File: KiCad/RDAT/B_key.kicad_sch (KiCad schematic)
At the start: 29 parts

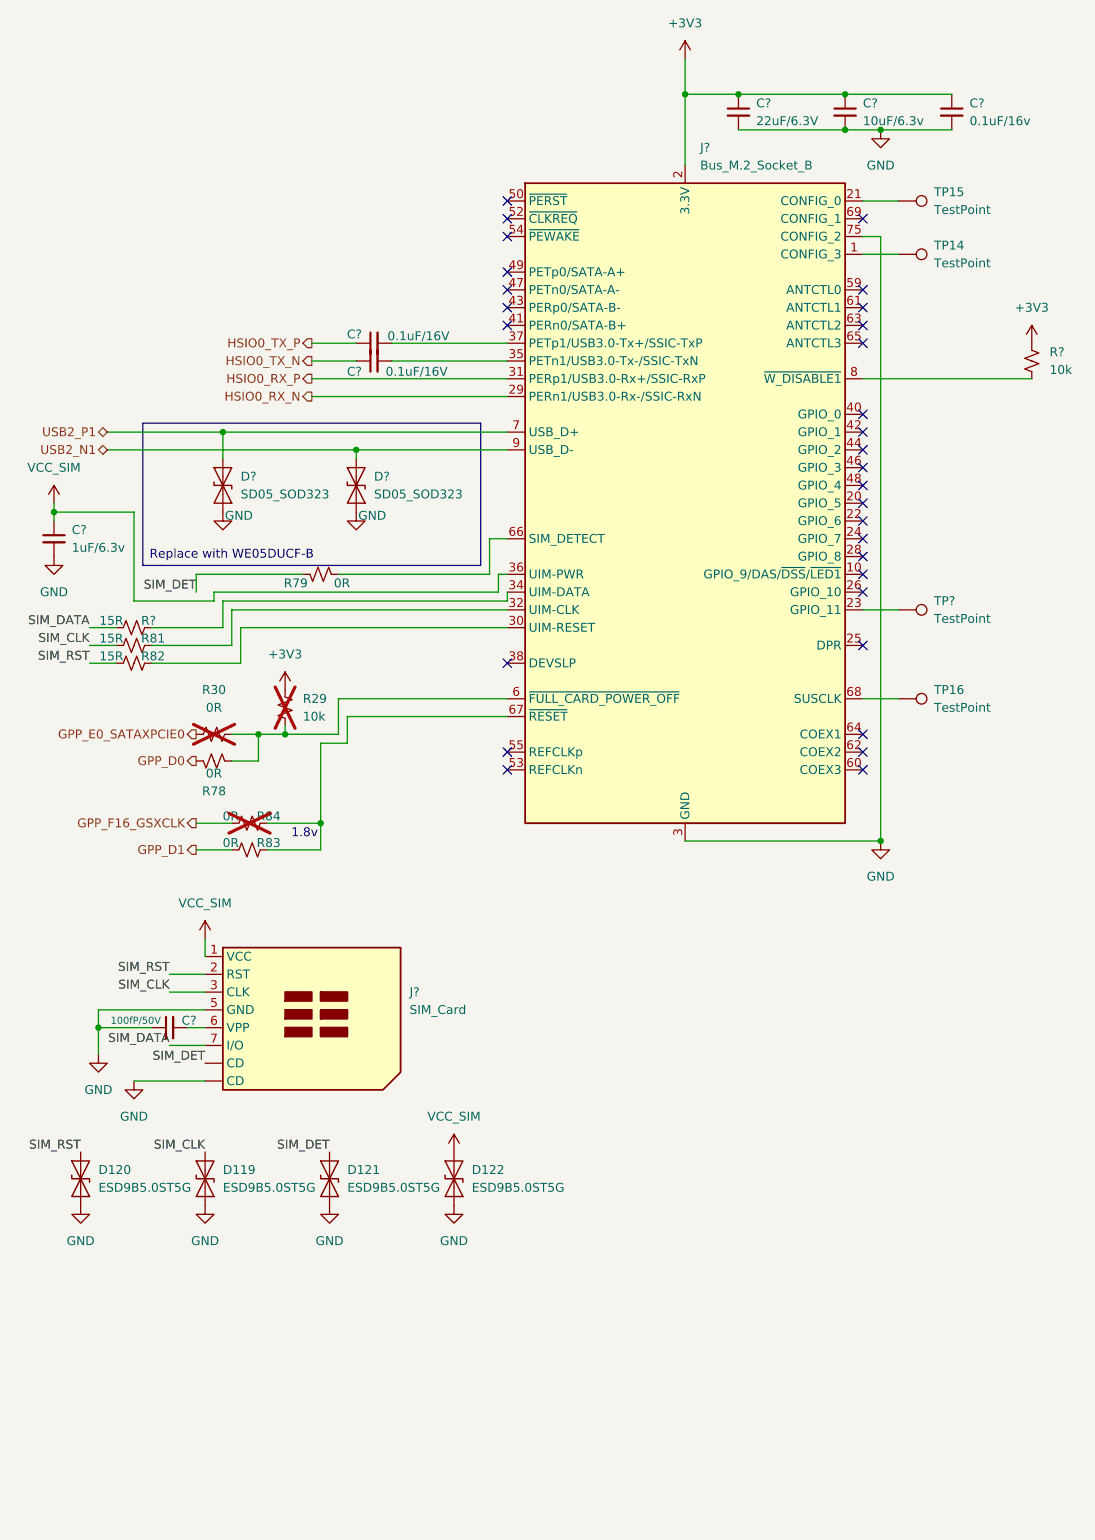
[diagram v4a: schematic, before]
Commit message: Added Libs and DOCS
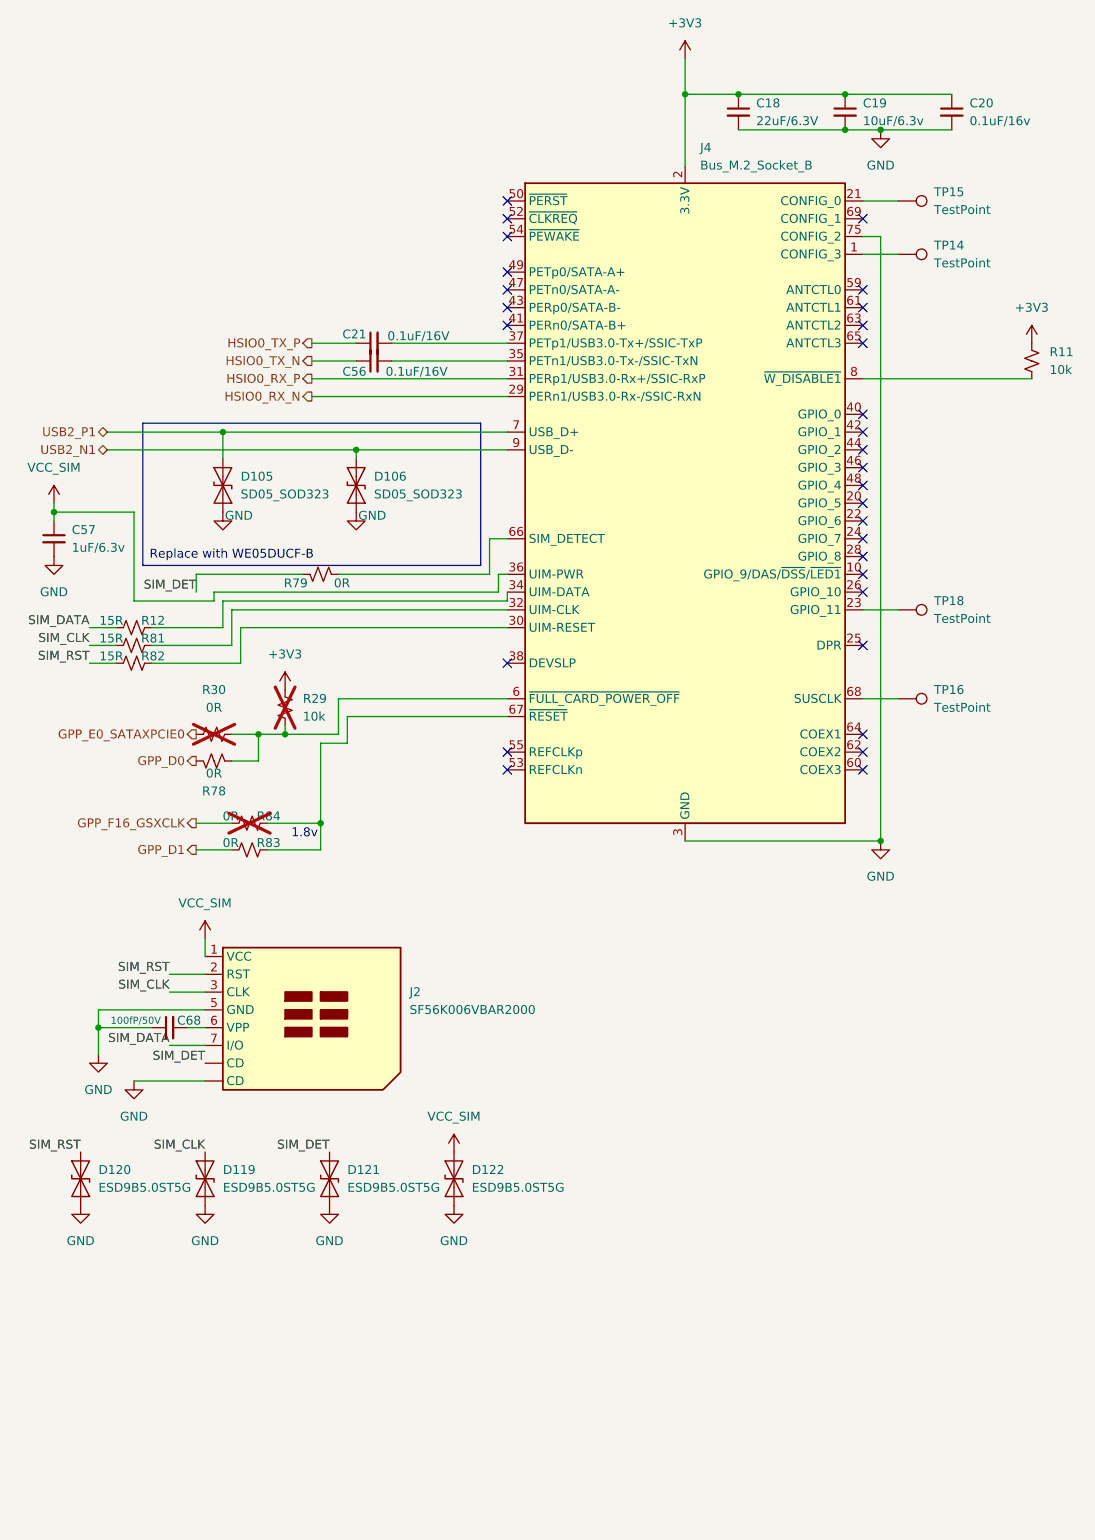
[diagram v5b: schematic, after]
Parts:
- J2: renamed from J?; value SIM_Card -> SF56K006VBAR2000; footprint (none) -> footprints:SF72S006VBDR2500_JAE; JLCPCB_LINK (none) -> https://jlcpcb.com/partdetail/JAEElectronics-SF56K006VBAR20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
- J4: renamed from J?; footprint (none) -> footprints:AMPHENOL_MDT420B03001; JLCPCB_LINK (none) -> https://jlcpcb.com/partdetail/AmphenolICC-MDT420B03001/C488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
- gave numbers to parts that had none: 12
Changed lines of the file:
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@@
 		(dnp no)
 		(fields_autoplaced yes)
-		(property "Reference" "#PWR?"
+		(property "Reference" "#PWR022"
 			(at 135.89 66.04 0)
 			(effects
@@
 			(project "RDAT"
 				(path "/0db9370a-8a21-4fd2-83a9-f207c3725dc9/55ec8a2f-3960-4a3a-93a6-0eefb6fdb74b"
-					(reference "#PWR?")
+					(reference "#PWR022")
 					(unit 1)
 				)
@@
 		(on_board yes)
 		(dnp no)
-		(property "Reference" "R?"
+		(property "Reference" "R12"
 			(at 30.226 130.556 90)
 			(effects
@@
 			(project "RDAT"
 				(path "/0db9370a-8a21-4fd2-83a9-f207c3725dc9/55ec8a2f-3960-4a3a-93a6-0eefb6fdb74b"
-					(reference "R?")
+					(reference "R12")
 					(unit 1)
 				)
@@
 		(dnp no)
 		(fields_autoplaced yes)
-		(property "Reference" "#PWR?"
+		(property "Reference" "#PWR023"
 			(at 157.48 93.98 0)
 			(effects
@@
 			(project "RDAT"
 				(path "/0db9370a-8a21-4fd2-83a9-f207c3725dc9/55ec8a2f-3960-4a3a-93a6-0eefb6fdb74b"
-					(reference "#PWR?")
+					(reference "#PWR023")
 					(unit 1)
 				)
@@
 		(dnp no)
 		(fields_autoplaced yes)
-		(property "Reference" "J?"
+		(property "Reference" "J4"
 			(at 110.0933 62.23 0)
 			(effects
@@
 			)
 		)
-		(property "Footprint" ""
+		(property "Footprint" "footprints:AMPHENOL_MDT420B03001"
 			(at 107.95 86.36 0)
 			(effects
@@
 			)
 		)
-		(property "JLCPCB_LINK" ""
+		(property "JLCPCB_LINK" "https://jlcpcb.com/partdetail/AmphenolICC-MDT420B03001/C4885179"
 			(at 107.95 113.03 0)
 			(effects
@@
 					(size 1.27 1.27)
 				)
+				(hide yes)
 			)
 		)
@@
 			(project "RDAT"
 				(path "/0db9370a-8a21-4fd2-83a9-f207c3725dc9/55ec8a2f-3960-4a3a-93a6-0eefb6fdb74b"
-					(reference "J?")
+					(reference "J4")
 					(unit 1)
 				)
@@
 		(dnp no)
 		(fields_autoplaced yes)
-		(property "Reference" "D?"
+		(property "Reference" "D106"
 			(at 63.5 109.2199 90)
 			(effects
@@
 			(project "RDAT"
 				(path "/0db9370a-8a21-4fd2-83a9-f207c3725dc9/55ec8a2f-3960-4a3a-93a6-0eefb6fdb74b"
-					(reference "D?")
+					(reference "D106")
 					(unit 1)
 				)
@@
 		(dnp no)
 		(fields_autoplaced yes)
-		(property "Reference" "J?"
+		(property "Reference" "J2"
 			(at 68.58 182.8799 0)
 			(effects
@@
 			)
 		)
-		(property "Value" "SIM_Card"
+		(property "Value" "SF56K006VBAR2000"
 			(at 68.58 185.4199 0)
 			(effects
@@
 			)
 		)
-		(property "Footprint" ""
+		(property "Footprint" "footprints:SF72S006VBDR2500_JAE"
 			(at 52.07 176.53 0)
 			(effects
@@
 			)
 		)
-		(property "Datasheet" "~"
+		(property "Datasheet" "https://wmsc.lcsc.com/wmsc/upload/file/pdf/v2/lcsc/2302091809_JAE-Electronics-SF56K006VBAR2000_C5357112.pdf"
 			(at 50.8 185.42 0)
 			(effects
@@
 			)
 		)
-		(property "JLCPCB_LINK" ""
+		(property "JLCPCB_LINK" "https://jlcpcb.com/partdetail/JAEElectronics-SF56K006VBAR2000/C5357112"
 			(at 52.07 185.42 0)
 			(effects
@@
 					(size 1.27 1.27)
 				)
+				(hide yes)
 			)
 		)
@@
 			(project "RDAT"
 				(path "/0db9370a-8a21-4fd2-83a9-f207c3725dc9/55ec8a2f-3960-4a3a-93a6-0eefb6fdb74b"
-					(reference "J?")
+					(reference "J2")
 					(unit 1)
 				)
@@
 		(dnp no)
 		(fields_autoplaced yes)
-		(property "Reference" "C?"
+		(property "Reference" "C18"
 			(at 118.11 55.8862 0)
 			(effects
@@
 			(project "RDAT"
 				(path "/0db9370a-8a21-4fd2-83a9-f207c3725dc9/55ec8a2f-3960-4a3a-93a6-0eefb6fdb74b"
-					(reference "C?")
+					(reference "C18")
 					(unit 1)
 				)
@@
 		(dnp no)
 		(fields_autoplaced yes)
-		(property "Reference" "C?"
+		(property "Reference" "C19"
 			(at 133.35 55.8862 0)
 			(effects
@@
 			(project "RDAT"
 				(path "/0db9370a-8a21-4fd2-83a9-f207c3725dc9/55ec8a2f-3960-4a3a-93a6-0eefb6fdb74b"
-					(reference "C?")
+					(reference "C19")
 					(unit 1)
 				)
@@
 		(dnp no)
 		(fields_autoplaced yes)
-		(property "Reference" "#PWR?"
+		(property "Reference" "#PWR028"
 			(at 135.89 167.64 0)
 			(effects
@@
 			(project "RDAT"
 				(path "/0db9370a-8a21-4fd2-83a9-f207c3725dc9/55ec8a2f-3960-4a3a-93a6-0eefb6fdb74b"
-					(reference "#PWR?")
+					(reference "#PWR028")
 					(unit 1)
 				)
@@
 		(dnp no)
 		(fields_autoplaced yes)
-		(property "Reference" "#PWR?"
+		(property "Reference" "#PWR024"
 			(at 17.78 116.84 0)
 			(effects
@@
 			(project "RDAT"
 				(path "/0db9370a-8a21-4fd2-83a9-f207c3725dc9/55ec8a2f-3960-4a3a-93a6-0eefb6fdb74b"
-					(reference "#PWR?")
+					(reference "#PWR024")
 					(unit 1)
 				)
@@
 		(dnp no)
 		(fields_autoplaced yes)
-		(property "Reference" "#PWR?"
+		(property "Reference" "#PWR027"
 			(at 17.78 127 0)
 			(effects
@@
 			(project "RDAT"
 				(path "/0db9370a-8a21-4fd2-83a9-f207c3725dc9/55ec8a2f-3960-4a3a-93a6-0eefb6fdb74b"
-					(reference "#PWR?")
+					(reference "#PWR027")
 					(unit 1)
 				)
@@
 		(dnp no)
 		(fields_autoplaced yes)
-		(property "Reference" "C?"
+		(property "Reference" "C57"
 			(at 20.32 116.8462 0)
 			(effects
@@
 			(project "RDAT"
 				(path "/0db9370a-8a21-4fd2-83a9-f207c3725dc9/55ec8a2f-3960-4a3a-93a6-0eefb6fdb74b"
-					(reference "C?")
+					(reference "C57")
 					(unit 1)
 				)
@@
 		(dnp no)
 		(fields_autoplaced yes)
-		(property "Reference" "C?"
+		(property "Reference" "C20"
 			(at 148.59 55.8862 0)
 			(effects
@@
 			(project "RDAT"
 				(path "/0db9370a-8a21-4fd2-83a9-f207c3725dc9/55ec8a2f-3960-4a3a-93a6-0eefb6fdb74b"
-					(reference "C?")
+					(reference "C20")
 					(unit 1)
 				)
@@
 		(on_board yes)
 		(dnp no)
-		(property "Reference" "C?"
+		(property "Reference" "C56"
 			(at 60.706 94.234 90)
 			(effects
@@
 			(project "RDAT"
 				(path "/0db9370a-8a21-4fd2-83a9-f207c3725dc9/55ec8a2f-3960-4a3a-93a6-0eefb6fdb74b"
-					(reference "C?")
+					(reference "C56")
 					(unit 1)
 				)
@@
 		(dnp no)
 		(fields_autoplaced yes)
-		(property "Reference" "D?"
+		(property "Reference" "D105"
 			(at 44.45 109.2199 90)
 			(effects
@@
 			(project "RDAT"
 				(path "/0db9370a-8a21-4fd2-83a9-f207c3725dc9/55ec8a2f-3960-4a3a-93a6-0eefb6fdb74b"
-					(reference "D?")
+					(reference "D105")
 					(unit 1)
 				)
@@
 		(dnp no)
 		(fields_autoplaced yes)
-		(property "Reference" "R?"
+		(property "Reference" "R11"
 			(at 160.02 91.4399 0)
 			(effects
@@
 			(project "RDAT"
 				(path "/0db9370a-8a21-4fd2-83a9-f207c3725dc9/55ec8a2f-3960-4a3a-93a6-0eefb6fdb74b"
-					(reference "R?")
+					(reference "R11")
 					(unit 1)
 				)
@@
 		(on_board yes)
 		(dnp no)
-		(property "Reference" "C?"
+		(property "Reference" "C21"
 			(at 60.706 88.9 90)
 			(effects
@@
 			(project "RDAT"
 				(path "/0db9370a-8a21-4fd2-83a9-f207c3725dc9/55ec8a2f-3960-4a3a-93a6-0eefb6fdb74b"
-					(reference "C?")
+					(reference "C21")
 					(unit 1)
 				)
@@
 		(dnp no)
 		(fields_autoplaced yes)
-		(property "Reference" "TP?"
+		(property "Reference" "TP18"
 			(at 143.51 126.9999 90)
 			(effects
@@
 			(project "RDAT"
 				(path "/0db9370a-8a21-4fd2-83a9-f207c3725dc9/55ec8a2f-3960-4a3a-93a6-0eefb6fdb74b"
-					(reference "TP?")
+					(reference "TP18")
 					(unit 1)
 				)
@@
 		(on_board yes)
 		(dnp no)
-		(property "Reference" "#PWR?"
+		(property "Reference" "#PWR025"
 			(at 41.91 120.65 0)
 			(effects
@@
 			(project "RDAT"
 				(path "/0db9370a-8a21-4fd2-83a9-f207c3725dc9/55ec8a2f-3960-4a3a-93a6-0eefb6fdb74b"
-					(reference "#PWR?")
+					(reference "#PWR025")
 					(unit 1)
 				)
@@
 		(on_board yes)
 		(dnp no)
-		(property "Reference" "C?"
+		(property "Reference" "C68"
 			(at 37.084 186.944 90)
 			(effects
@@
 			(project "RDAT"
 				(path "/0db9370a-8a21-4fd2-83a9-f207c3725dc9/55ec8a2f-3960-4a3a-93a6-0eefb6fdb74b"
-					(reference "C?")
+					(reference "C68")
 					(unit 1)
 				)
@@
 		(on_board yes)
 		(dnp no)
-		(property "Reference" "#PWR?"
+		(property "Reference" "#PWR026"
 			(at 60.96 120.65 0)
 			(effects
@@
 			(project "RDAT"
 				(path "/0db9370a-8a21-4fd2-83a9-f207c3725dc9/55ec8a2f-3960-4a3a-93a6-0eefb6fdb74b"
-					(reference "#PWR?")
-					(unit 1)
-				)
+					(reference "#PWR026")
+					(unit 1)
+				)

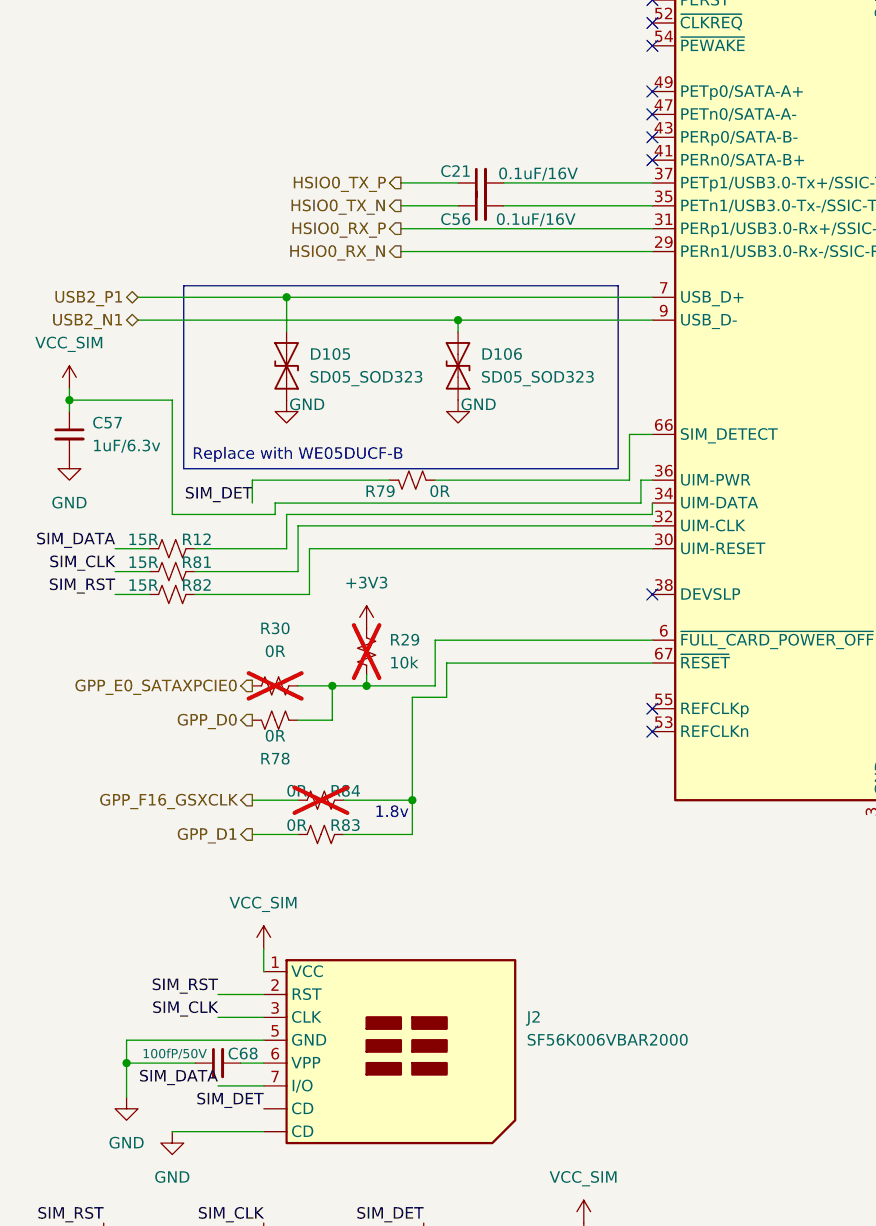
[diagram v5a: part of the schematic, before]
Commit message: Sourced and documented all parts
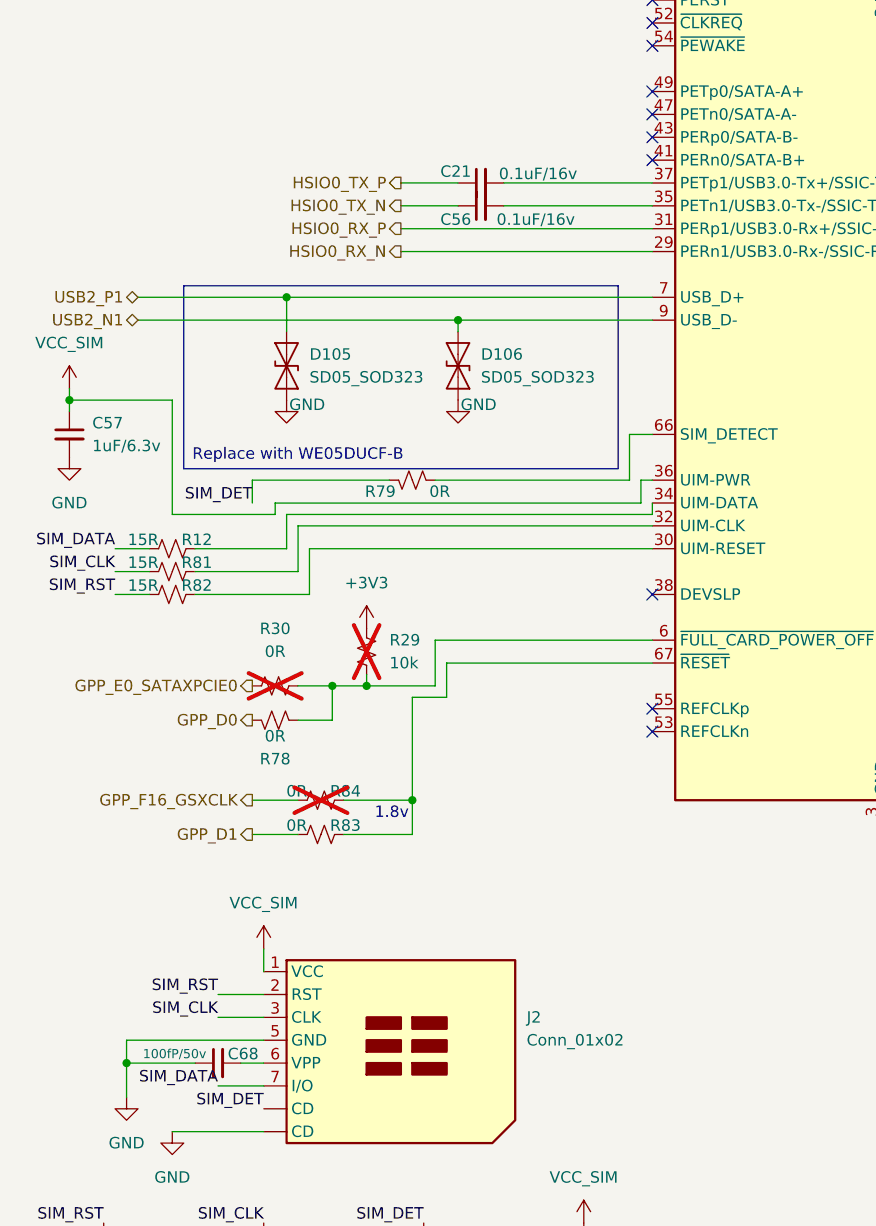
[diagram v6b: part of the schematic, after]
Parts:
- C18: footprint (none) -> Capacitor_SMD:C_0402_1005Metric; JLCPCB_LINK (none) -> https://jlcpcb.com/partdetail/4414076-GRM158R61A226ME15D/C3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
- C19: footprint (none) -> Capacitor_SMD:C_0402_1005Metric; JLCPCB_LINK (none) -> https://jlcpcb.com/partdetail/16204-CL05A106MQ5NUNC/C15525
- C20: footprint (none) -> Capacitor_SMD:C_0402_1005Metric; JLCPCB_LINK (none) -> https://jlcpcb.com/partdetail/1933-0402F104M500NT/C1581
- C21, C56: value 0.1uF/16V -> 0.1uF/16v; footprint (none) -> Capacitor_SMD:C_0402_1005Metric; JLCPCB_LINK (none) -> https://jlcpcb.com/partdetail/1933-0402F104M500NT/C1581
- C57: footprint (none) -> Capacitor_SMD:C_0402_1005Metric; JLCPCB_LINK (none) -> https://jlcpcb.com/partdetail/1877-CL05B104KO5NNNC/C1525
- C68: value 100fP/50V -> 100fP/50v; footprint (none) -> Capacitor_SMD:C_0402_1005Metric; JLCPCB_LINK (none) -> https://jlcpcb.com/partdetail/27153-CL05C101JB5NNNC/C26409
- D105, D106: JLCPCB_LINK (none) -> https://jlcpcb.com/partdetail/2790626-PSD05C_LFT7/C2687123
- D119, D120, D121, D122: JLCPCB_LINK (none) -> https://jlcpcb.com/partdetail/TechPublic-TPESD9B50ST5G/C268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
- J2: value SF56K006VBAR2000 -> Conn_01x02; footprint footprints:SF72S006VBDR2500_JAE -> Connector_PinHeader_1.00mm:PinHeader_1x02_P1.00mm_Vertical; JLCPCB_LINK https://jlcpcb.com/partdetail/JAEElectronics-SF56K006VBAR20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 -> https://www.digikey.com/en/products/detail/gct/BC020-02-A-0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
- R11: JLCPCB_LINK (none) -> https://jlcpcb.com/partdetail/26487-0402WGF1002TCE/C25744
- R12, R81, R82: footprint (none) -> Resistor_SMD:R_0402_1005Metric; JLCPCB_LINK (none) -> https://jlcpcb.com/partdetail/25826-0402WGF150JTCE/C25083
- R78, R79, R83: footprint (none) -> Resistor_SMD:R_0402_1005Metric; JLCPCB_LINK (none) -> https://jlcpcb.com/partdetail/17853-0402WGF0000TCE/C17168
- TP14, TP15, TP16, TP18: footprint (none) -> TestPoint:TestPoint_Pad_1.0x1.0mm

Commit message: Push before Board Layout
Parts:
- R11, R29, R30, R84: footprint (none) -> Resistor_SMD:R_0402_1005Metric
- renumbered J2 to J3
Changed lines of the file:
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@@
 			)
 		)
-		(property "Footprint" ""
+		(property "Footprint" "Resistor_SMD:R_0402_1005Metric"
 			(at 40.64 146.05 0)
 			(effects
@@
 		(dnp no)
 		(fields_autoplaced yes)
-		(property "Reference" "J2"
+		(property "Reference" "J3"
 			(at 68.58 182.8799 0)
 			(effects
@@
 			(project "RDAT"
 				(path "/0db9370a-8a21-4fd2-83a9-f207c3725dc9/55ec8a2f-3960-4a3a-93a6-0eefb6fdb74b"
-					(reference "J2")
+					(reference "J3")
 					(unit 1)
 				)
@@
 			)
 		)
-		(property "Footprint" ""
+		(property "Footprint" "Resistor_SMD:R_0402_1005Metric"
 			(at 50.8 142.24 0)
 			(effects
@@
 			)
 		)
-		(property "Footprint" ""
+		(property "Footprint" "Resistor_SMD:R_0402_1005Metric"
 			(at 157.48 92.71 0)
 			(effects
@@
 			)
 		)
-		(property "Footprint" ""
+		(property "Footprint" "Resistor_SMD:R_0402_1005Metric"
 			(at 45.72 158.75 0)
 			(effects
